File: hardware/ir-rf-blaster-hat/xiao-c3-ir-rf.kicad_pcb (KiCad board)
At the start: 2 copper layers, 21 x 50 mm, 18 parts, among them J1 XIAO_SOCKET_1x7, J2 XIAO_SOCKET_1x7, M1 CC1101_MODULE, Q1 SOT-23

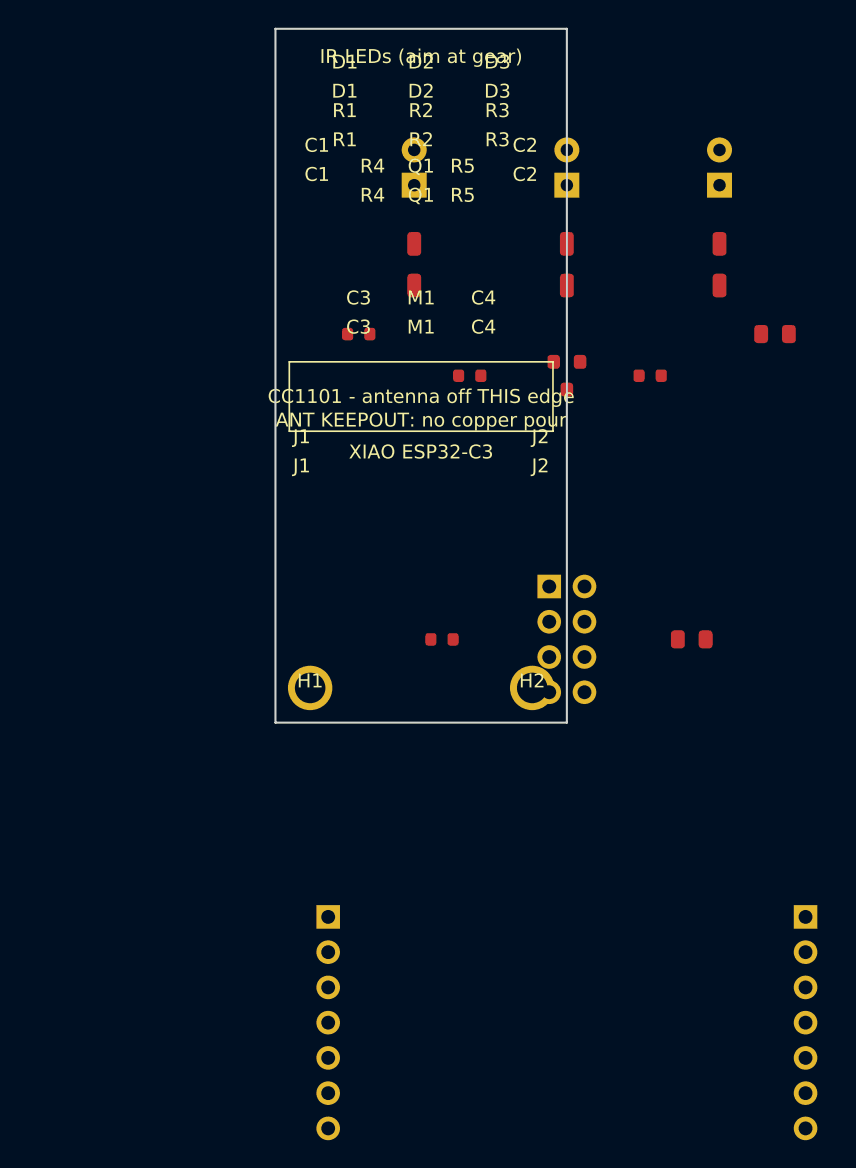
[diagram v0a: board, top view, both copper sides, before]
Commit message: feat(ir-rf-blaster): 4-layer, fully-routed, DRC-clean board
Rebuild the XIAO IR+RF blaster hat as a 4-layer board, generated headlessly:
- Stackup F.Cu / In1.Cu GND plane / In2.Cu +5V plane / B.Cu. Real KiCad library
  footprints (was crude embedded geometry). GND/+5V stitched to planes via
  through-vias; +3V3 and logic signals routed on the outer layers.
- SPI fan-out uses a monotonic XIAO->CC1101 pin mapping so the traces don't cross.
- Validated with kicad-cli (KiCad 9): DRC 0 errors, 0 unconnected. Board 22x50mm.
- Ships generate_pcb.py (kiutils), fill_zones.py (pcbnew LoadBoard), the 8 footprints
  (offline-reproducible), the filled .kicad_pcb, a top render, and Gerbers/drill.

pcbnew scripting crashes under amd64 emulation on Apple Silicon (FootprintLoad), so
generation uses kiutils and zone-fill uses pcbnew.LoadBoard (which doesn't crash);
kicad-cli does DRC/export. Documented in the README.

Still GUI TODOs (flagged): swap the provisional XIAO socket for Seeed's official
footprint, and add the antenna copper keepout for the specific CC1101 module.

Co-Authored-By: Claude Opus 4.8 <noreply@anthropic.com>
Claude-Session: https://claude.ai/code/session_01NfkRErMrPyNuft1RbpzMet
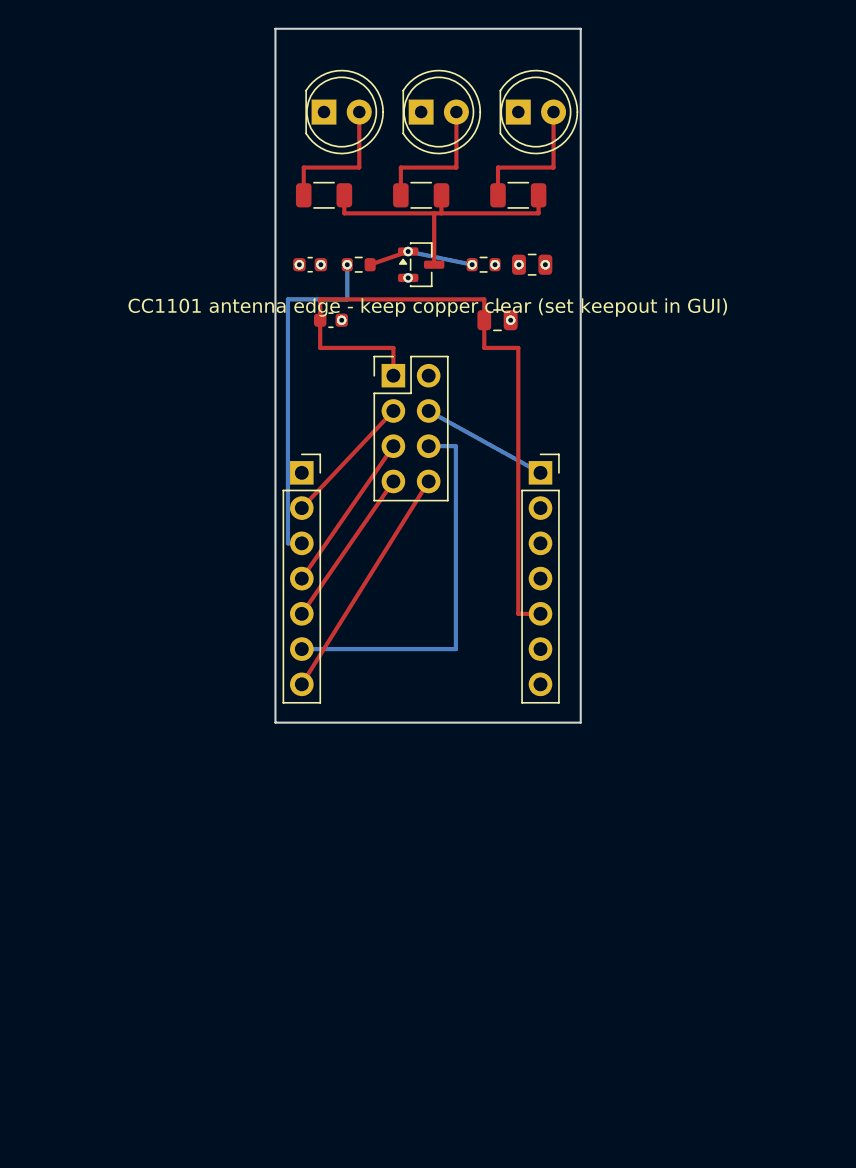
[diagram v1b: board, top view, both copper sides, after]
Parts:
- removed H1, H2: M2, hat:MountingHole_M2
- C1, C3: value C_0603 -> 100nF; footprint hat:C_0603 -> C_0603_1608Metric
- C2: value C_0805 -> 22uF; footprint hat:C_0805 -> C_0805_2012Metric
- C4: value C_0805 -> 10uF; footprint hat:C_0805 -> C_0805_2012Metric
- D1, D2, D3: value LED_D5.0mm -> 940nm; footprint hat:LED_D5.0mm -> LED_D5.0mm
- J1: value XIAO_SOCKET_1x7 -> XIAO_L; footprint hat:XIAO_SOCKET_1x7 -> PinSocket_1x07_P2.54mm_Vertical
- J2: value XIAO_SOCKET_1x7 -> XIAO_R; footprint hat:XIAO_SOCKET_1x7 -> PinSocket_1x07_P2.54mm_Vertical
- M1: value CC1101_MODULE -> CC1101; footprint hat:CC1101_MODULE -> PinHeader_2x04_P2.54mm_Vertical
- Q1: value SOT-23 -> AO3400A; footprint hat:SOT-23 -> SOT-23
- R1, R2, R3: value R_1206 -> 15R; footprint hat:R_1206 -> R_1206_3216Metric
- R4: value R_0603 -> 100R; footprint hat:R_0603 -> R_0603_1608Metric
- R5: value R_0603 -> 10k; footprint hat:R_0603 -> R_0603_1608Metric
- moved C1 6.02 mm to (2.50, 17.0)
- moved C2 6.02 mm to (18.5, 17.0)
- moved R5 4.74 mm to (15.0, 17.0)
- moved R4 4.61 mm to (6.00, 17.0)
- moved Q1 4.50 mm to (10.5, 17.0)
- moved R1 3.81 mm to (3.50, 12.0)
- moved R3 3.81 mm to (17.5, 12.0)
- moved M1 3.61 mm to (8.50, 25.0)
- moved R2 3.50 mm to (10.5, 12.0)
- moved C3 2.24 mm to (4.00, 21.0)
- moved D1 1.80 mm to (3.50, 6.00)
- moved D3 1.80 mm to (17.5, 6.00)
- moved C4 1.41 mm to (16.0, 21.0)
- moved D2 1.00 mm to (10.5, 6.00)
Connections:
- M1 pad 3: CC_SCK -> CC_GDO2
- M1 pad 4: CC_MOSI -> CC_MISO
- M1 pad 5: CC_MISO -> CC_CSN
- M1 pad 6: CC_CSN -> CC_SCK
- M1 pad 8: CC_GDO2 -> CC_MOSI
- Q1 pad 1: IR_TX -> Q_GATE
- R4 pad 2: IR_TX -> Q_GATE
- R5 pad 1: IR_TX -> Q_GATE
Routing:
- net +3V3: track 0.00 -> 49.3 mm
- net CC_SCK: track 0.00 -> 27.7 mm
- net IR_TX: track 0.00 -> 25.4 mm, vias 0 -> 1
- net Q_DRAIN: track 0.00 -> 21.6 mm
- net CC_MOSI: track 0.00 -> 17.2 mm
- net CC_GDO0: track 0.00 -> 11.6 mm
- net CC_CSN: track 0.00 -> 11.6 mm
- net LED2_K: track 0.00 -> 10.0 mm
- net LED1_K: track 0.00 -> 10.0 mm
- net LED3_K: track 0.00 -> 10.0 mm
- net CC_GDO2: track 0.00 -> 9.62 mm
- net CC_MISO: track 0.00 -> 9.21 mm
- net Q_GATE: track 0.00 -> 7.61 mm, vias 0 -> 2
- net GND: vias 0 -> 6
- net +5V: vias 0 -> 2
- added copper zone on In2.Cu, net +5V
- added copper zone on In1.Cu, net GND
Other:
- board size 21 x 50 mm -> 22 x 50 mm
- copper layers 2 -> 4
- rule pad_to_mask_clearance: 0.0 -> 0
- board text added: "CC1101 antenna edge - keep copper clear (set keepout in GUI)"
- board text removed: "ANT KEEPOUT: no copper pour"
- board text removed: "C1"
- board text removed: "C2"
- board text removed: "C3"
- board text removed: "C4"
- board text removed: "CC1101 - antenna off THIS edge"
- board text removed: "D1"
- board text removed: "D2"
- board text removed: "D3"
- board text removed: "IR LEDs (aim at gear)"
- board text removed: "J1"
- board text removed: "J2"
- board text removed: "M1"
- board text removed: "Q1"
- board text removed: "R1"
- board text removed: "R2"
- board text removed: "R3"
- board text removed: "R4"
- board text removed: "R5"
- board text removed: "XIAO ESP32-C3"

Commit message: refactor(ir-rf-blaster): straighter, 45-degree, centered routing
- Straight diagonals where the line is clear (LED cathodes; SPI fan is already
  straight parallel), 45-degree chamfers on the rest (no 90-degree turns).
- Components centered east-west about the board centerline (x=11).
- Simplified the +3V3 tail to XIAO 3V3: straight drop + one 45-degree bend.
Still DRC-clean (0 errors, 0 unconnected). Re-exported Gerbers + render.

Co-Authored-By: Claude Opus 4.8 <noreply@anthropic.com>
Claude-Session: https://claude.ai/code/session_01NfkRErMrPyNuft1RbpzMet
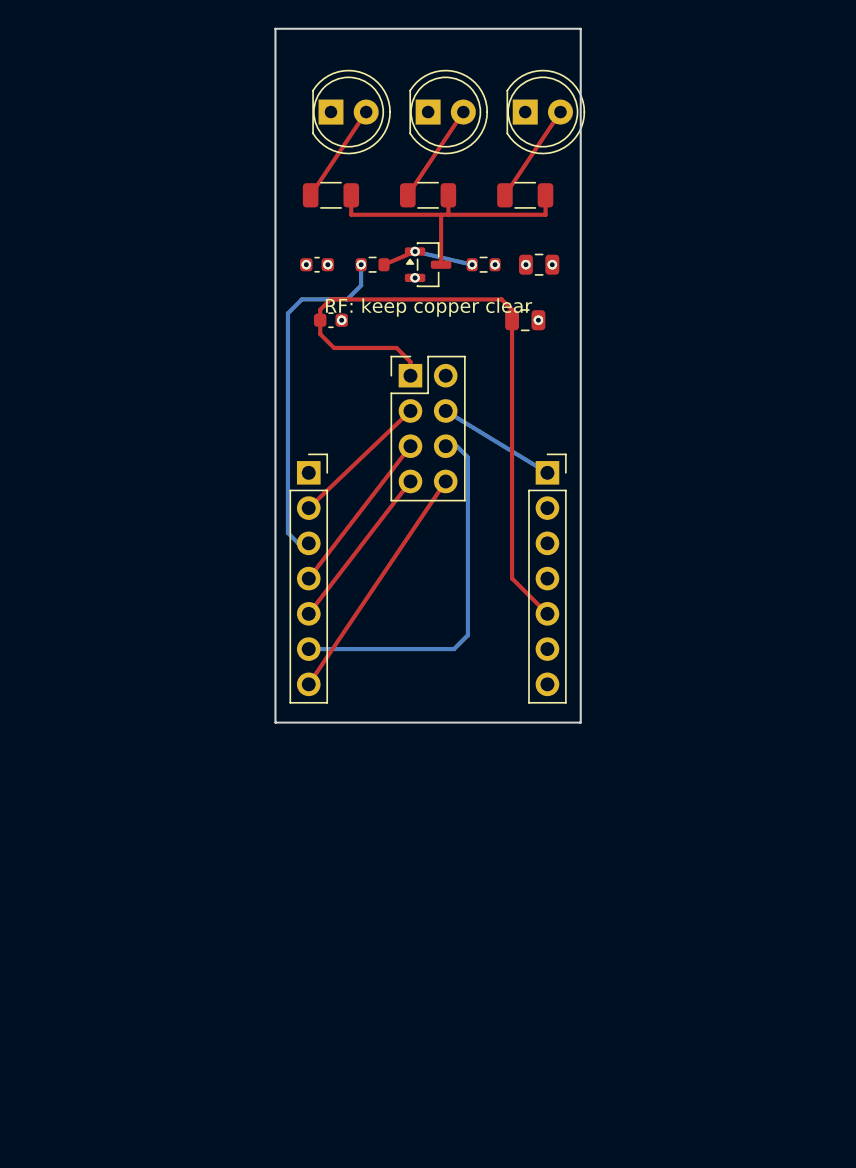
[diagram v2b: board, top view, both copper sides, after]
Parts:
- moved C4 2.00 mm to (18.0, 21.0)
- moved M1 1.23 mm to (9.73, 25.0)
- moved R4 1.00 mm to (7.00, 17.0)
- moved C1 0.50 mm to (3.00, 17.0)
- moved C2 0.50 mm to (19.0, 17.0)
- moved D1 0.50 mm to (4.00, 6.00)
- moved D2 0.50 mm to (11.0, 6.00)
- moved D3 0.50 mm to (18.0, 6.00)
- moved J1 0.50 mm to (2.40, 32.0)
- moved J2 0.50 mm to (19.6, 32.0)
- moved Q1 0.50 mm to (11.0, 17.0)
- moved R1 0.50 mm to (4.00, 12.0)
- moved R2 0.50 mm to (11.0, 12.0)
- moved R3 0.50 mm to (18.0, 12.0)
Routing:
- net LED3_K: track 10.0 -> 7.21 mm
- net LED2_K: track 10.0 -> 7.21 mm
- net LED1_K: track 10.0 -> 7.21 mm
- net +3V3: track 49.3 -> 47.5 mm
- net CC_SCK: track 27.7 -> 26.6 mm
- net Q_GATE: track 7.61 -> 6.65 mm
- net CC_MISO: track 9.21 -> 8.58 mm
- net CC_GDO2: track 9.62 -> 10.1 mm
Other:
- board text added: "RF: keep copper clear"
- board text removed: "CC1101 antenna edge - keep copper clear (set keepout in GUI)"

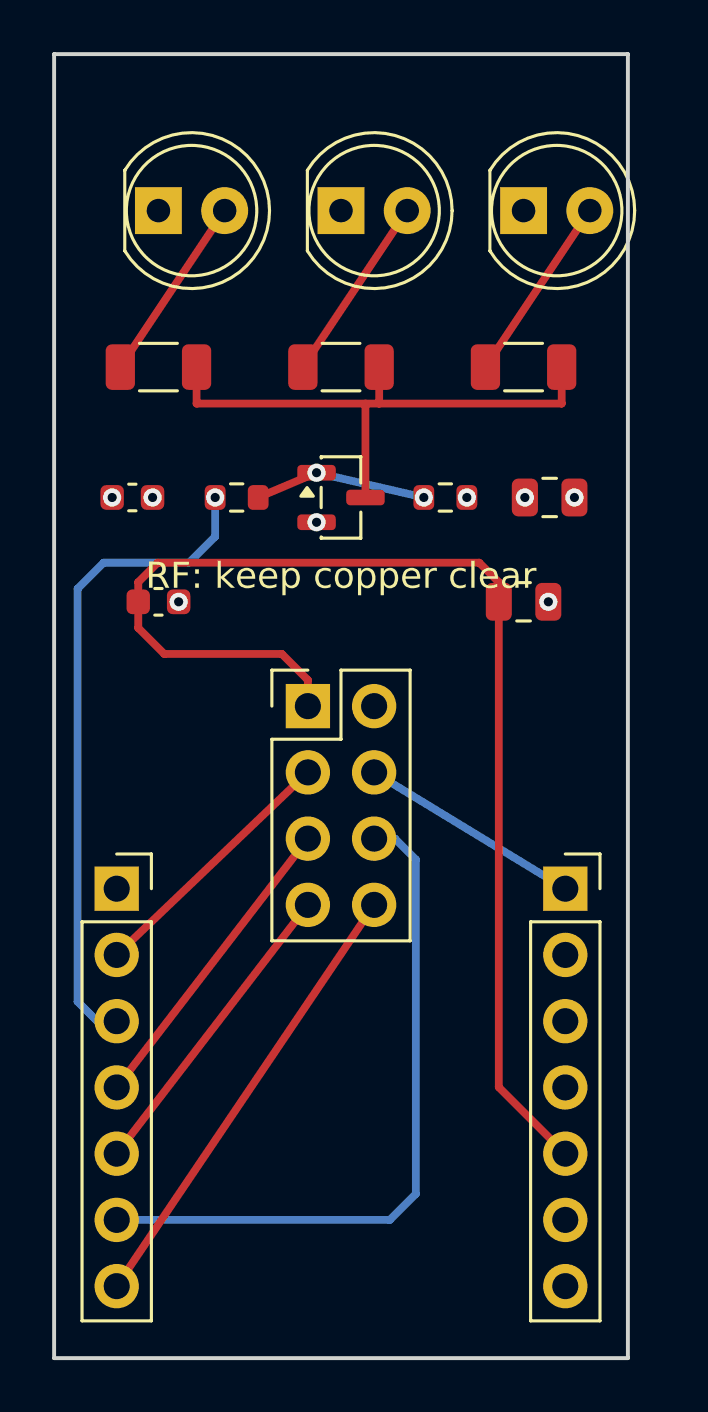
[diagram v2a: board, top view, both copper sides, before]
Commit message: fix(ir-rf-blaster): center LEDs on board, fix off-board silk
Widen board to 23mm and center all components on the x=11.5 centerline so the
outer LEDs have proper edge margin (was clipping D3's silk off the right edge).
Dropped the RF silk note (it overlapped the caps; keepout is in the README).
DRC now 0 errors, 0 unconnected, 0 warnings. Re-exported Gerbers + render.

Co-Authored-By: Claude Opus 4.8 <noreply@anthropic.com>
Claude-Session: https://claude.ai/code/session_01NfkRErMrPyNuft1RbpzMet
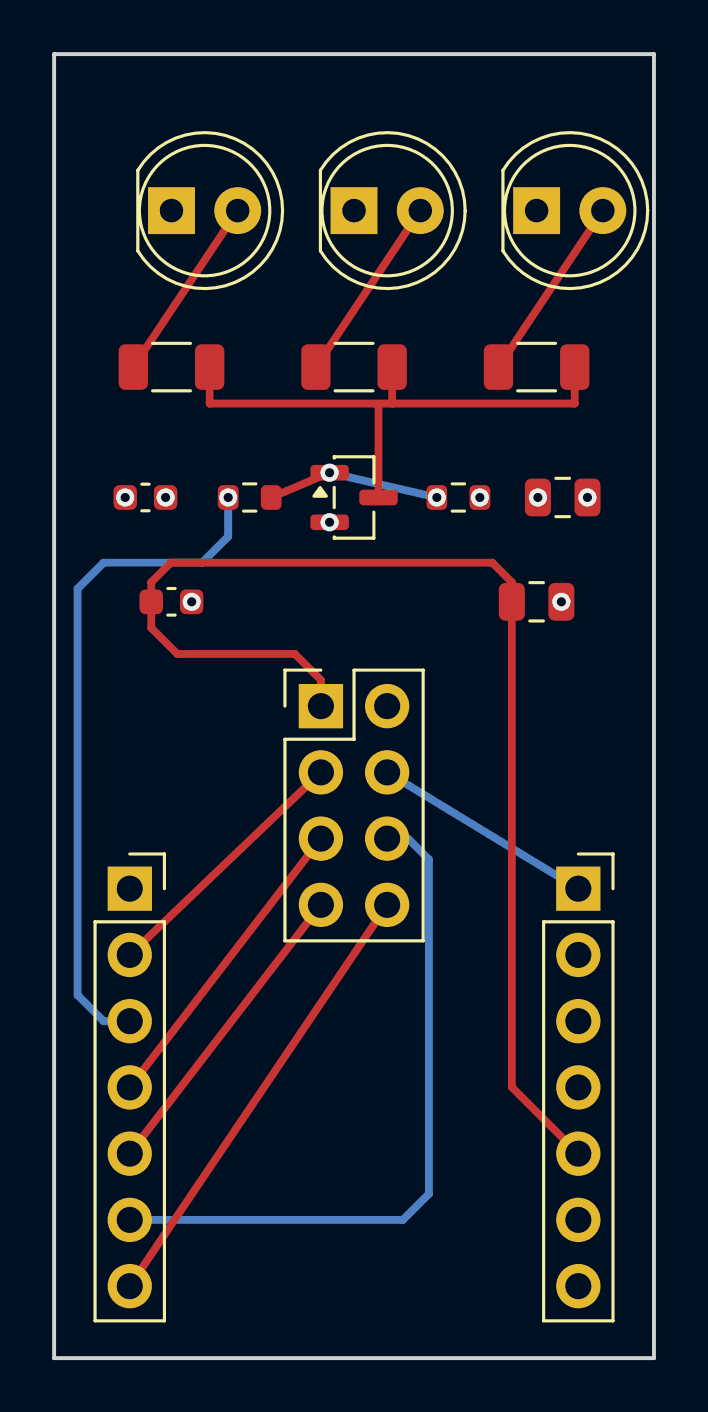
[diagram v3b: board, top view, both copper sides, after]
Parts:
- moved C1 0.50 mm to (3.50, 17.0)
- moved C2 0.50 mm to (19.5, 17.0)
- moved C3 0.50 mm to (4.50, 21.0)
- moved C4 0.50 mm to (18.5, 21.0)
- moved D1 0.50 mm to (4.50, 6.00)
- moved D2 0.50 mm to (11.5, 6.00)
- moved D3 0.50 mm to (18.5, 6.00)
- moved J1 0.50 mm to (2.90, 32.0)
- moved J2 0.50 mm to (20.1, 32.0)
- moved M1 0.50 mm to (10.2, 25.0)
- moved Q1 0.50 mm to (11.5, 17.0)
- moved R1 0.50 mm to (4.50, 12.0)
- moved R2 0.50 mm to (11.5, 12.0)
- moved R3 0.50 mm to (18.5, 12.0)
- moved R4 0.50 mm to (7.50, 17.0)
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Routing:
- net IR_TX: track 25.2 -> 26.1 mm
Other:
- board size 22 x 50 mm -> 23 x 50 mm
- board text removed: "RF: keep copper clear"

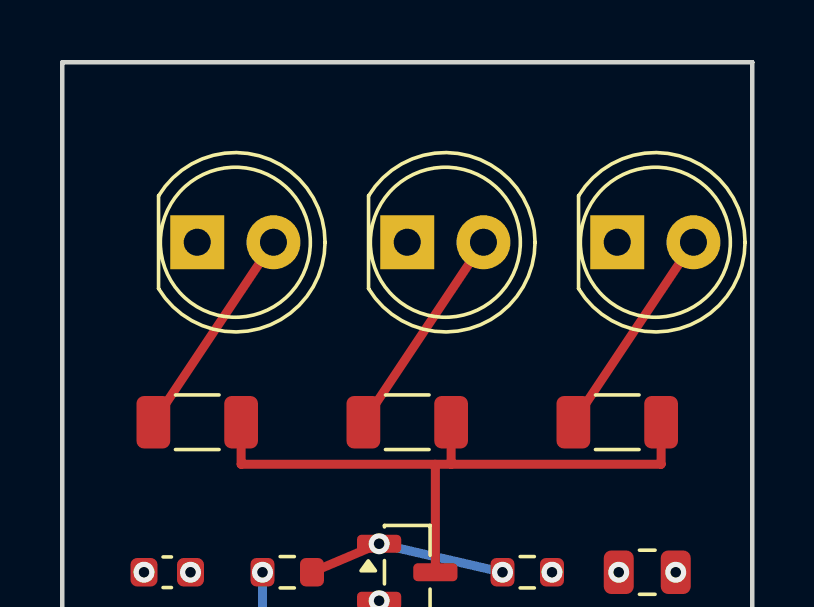
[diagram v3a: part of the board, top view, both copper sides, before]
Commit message: fix(ir-rf-blaster): center LED bodies (shift footprints left half a pin-gap)
The LED_D5.0mm origin is at pin 1, so the round body sat 1.27mm right of the
placement point. Shift the LED footprints left by 1.27mm (half the 2.54mm pin
gap) so the bodies center on their column and align with the resistors. Still
DRC-clean: 0 errors, 0 unconnected, 0 warnings.

Co-Authored-By: Claude Opus 4.8 <noreply@anthropic.com>
Claude-Session: https://claude.ai/code/session_01NfkRErMrPyNuft1RbpzMet
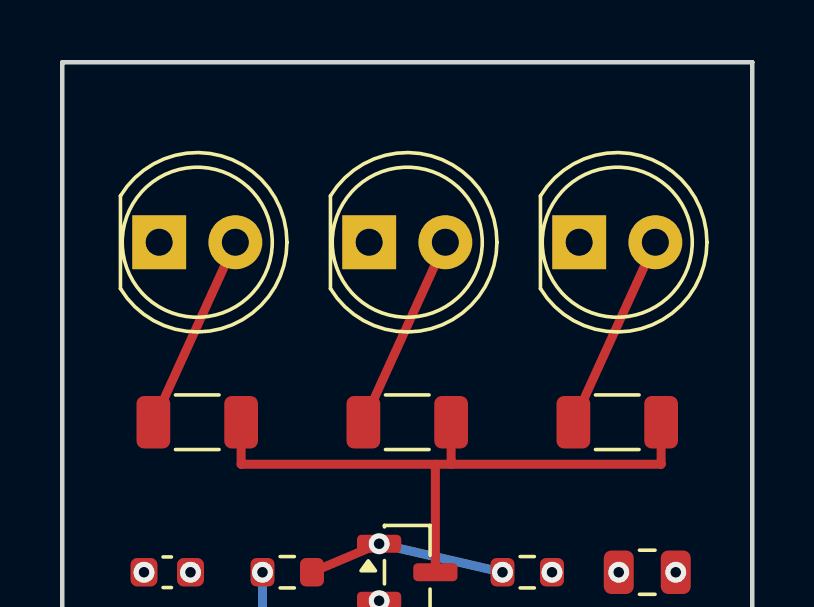
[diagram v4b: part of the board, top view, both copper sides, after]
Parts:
- moved D1 1.27 mm to (3.23, 6.00)
- moved D2 1.27 mm to (10.2, 6.00)
- moved D3 1.27 mm to (17.2, 6.00)
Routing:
- net LED2_K: track 7.21 -> 6.59 mm
- net LED1_K: track 7.21 -> 6.59 mm
- net LED3_K: track 7.21 -> 6.59 mm

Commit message: refactor(ir-rf-blaster): rotate LEDs 180 to straighten the cathode traces
Flip the LEDs so the cathode sits directly above the resistor's LED_K pad -> the
cathode traces drop nearly straight down instead of angling across. Body stays
centered (offset +1.27 instead of -1.27). Still DRC-clean: 0 errors, 0 unconnected.

Co-Authored-By: Claude Opus 4.8 <noreply@anthropic.com>
Claude-Session: https://claude.ai/code/session_01NfkRErMrPyNuft1RbpzMet
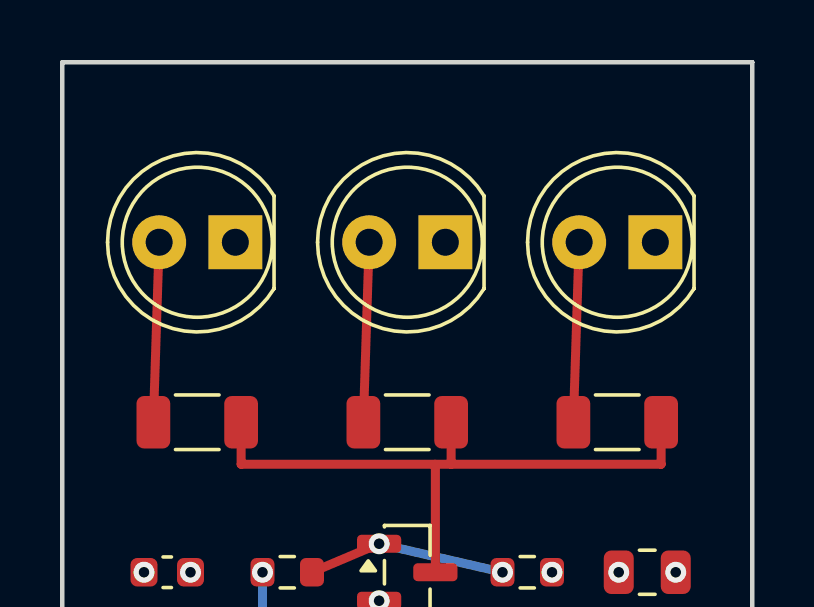
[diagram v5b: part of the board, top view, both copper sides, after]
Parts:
- moved D1 2.54 mm to (5.77, 6.00), turned to 180 degrees
- moved D2 2.54 mm to (12.8, 6.00), turned to 180 degrees
- moved D3 2.54 mm to (19.8, 6.00), turned to 180 degrees
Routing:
- net LED3_K: track 6.59 -> 6.00 mm
- net LED2_K: track 6.59 -> 6.00 mm
- net LED1_K: track 6.59 -> 6.00 mm
